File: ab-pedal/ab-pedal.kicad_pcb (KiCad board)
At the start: 2 copper layers, 52 x 70 mm, 24 parts, among them J2 IN, J3 OUT_A, J4 OUT_B, J5 IN_A, J6 IN_B, J7 OUT, J8 Jack-DC, SW1 TRUE_BYPASS, SW2 INVERT, SW3 ON, U1 TL074, U2 MAX1044

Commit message: layout
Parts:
- removed J3: OUT_A, Connector_Audio:Jack_6.35mm_Neutrik_NMJ6HFD2_Horizontal
- removed J5: IN_A, Connector_Audio:Jack_6.35mm_Neutrik_NMJ6HFD2_Horizontal
- added J1: PEDAL, Connector_Audio:Jack_6.35mm_Neutrik_NMJ6HFD2_Horizontal, B.Cu at (125.2, 123.7)
- C2, C4, C5: footprint Capacitor_THT:CP_Radial_D10.0mm_P5.00mm -> Capacitor_THT:CP_Radial_D4.0mm_P2.00mm
- J2, J7: moved to B.Cu
- J4: value OUT_B -> SEND; moved to B.Cu
- J6: value IN_B -> RECV; moved to B.Cu
- R1, R2, R3, R4, R5: footprint Resistor_THT:R_Axial_DIN0207_L6.3mm_D2.5mm_P10.16mm_Horizontal -> Resistor_THT:R_Axial_DIN0207_L6.3mm_D2.5mm_P5.08mm_Vertical
- SW3: footprint Connector_PinHeader_2.54mm:PinHeader_2x03_P2.54mm_Vertical -> _project:PinHeader_2x03_P2.54mm_Vertical
- moved SW3 187.5 mm to (55.9, 117.9), turned to 0 degrees
- moved D1 185.8 mm to (57.1, 106.4), turned to -90 degrees
- moved R5 179.4 mm to (61.8, 101.9), turned to 180 degrees
- moved J8 179.3 mm to (118.1, 119.9)
- moved R4 179.3 mm to (88.2, 104.1)
- moved C2 173.3 mm to (114.5, 121.2), turned to 180 degrees
- moved R3 171.0 mm to (97.1, 104.1)
- moved C5 161.8 mm to (108.7, 121.2)
- moved SW2 153.5 mm to (112.7, 87.1), turned to -90 degrees
- moved U1 148.1 mm to (98.3, 108.4), turned to -90 degrees
- moved C1 147.0 mm to (102.4, 109.8), turned to -90 degrees
- moved SW1 147.0 mm to (87.9, 87.3), turned to -90 degrees
- moved C3 144.2 mm to (118.1, 114.7), turned to 90 degrees
- moved R1 142.6 mm to (88.6, 120.3)
- moved R2 142.2 mm to (98.0, 120.3), turned to 0 degrees
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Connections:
- net IN_B renamed RETURN
- J2 pad R: (no net) -> GND
- J2 pad RN: (no net) -> GND
- J4 pad R: (no net) -> GND
- J4 pad RN: (no net) -> GND
- J4 pad T: OUT_A -> BUFFERED
- J6 pad R: (no net) -> GND
- J6 pad RN: (no net) -> GND
- J7 pad R: (no net) -> GND
- J7 pad RN: (no net) -> GND
- J7 pad TN: GND -> unconnected-(J7-PadTN)
- R1 pad 1: Net-(SW2B-A) -> Net-(SW2B-C)
- R1 pad 2: Net-(U1B--) -> Net-(U1D--)
- R2 pad 1: Net-(U1B--) -> Net-(U1D--)
- R2 pad 2: Net-(SW2A-A) -> Net-(SW2A-C)
- R3 pad 1: Net-(R3-Pad1) -> Net-(J1-PadR)
- R3 pad 2: Net-(U1C--) -> Net-(U1B--)
- R4 pad 1: Net-(U1C--) -> Net-(U1B--)
- RV1 pad 1: IN_A -> Net-(J1-PadSN)
- RV1 pad 2: Net-(R3-Pad1) -> Net-(J1-PadRN)
- RV1 pad 3: IN_B~ -> Net-(J1-PadTN)
- SW1 pad 1: IN_A -> Net-(SW1A-A)
- SW1 pad 2: Net-(SW1A-B) -> OUT
- SW1 pad 3: IN -> Net-(SW1A-C)
- SW1 pad 4: Net-(SW1B-A) -> BUFFERED
- SW1 pad 5: OUT -> Net-(SW1B-B)
- SW1 pad 6: Net-(SW1B-C) -> IN
- SW2 pad 2: IN_B~ -> RETURN~
- SW2 pad 4: Net-(SW2B-A) -> Net-(SW2A-A)
- SW2 pad 6: Net-(SW2A-C) -> Net-(SW2B-C)
- SW3 pad 1: BLEND -> Net-(D1-RK)
- SW3 pad 2: Net-(SW1B-C) -> GND
- SW3 pad 3: Net-(SW1A-B) -> Net-(D1-GK)
- SW3 pad 4: Net-(D1-RK) -> Net-(SW1B-B)
- SW3 pad 5: GND -> Net-(SW1A-C)
- SW3 pad 6: Net-(D1-GK) -> BLEND
- U1 pad 1: OUT_A -> Net-(SW1A-A)
- U1 pad 10: GND -> IN
- U1 pad 12: Net-(SW1B-C) -> GND
- U1 pad 13: Net-(SW1B-A) -> Net-(U1D--)
- U1 pad 14: Net-(SW1B-A) -> Net-(SW2A-C)
- U1 pad 2: OUT_A -> Net-(SW1A-A)
- U1 pad 3: IN -> Net-(SW1A-C)
- U1 pad 7: Net-(SW2A-A) -> BLEND
- U1 pad 8: BLEND -> BUFFERED
- U1 pad 9: Net-(U1C--) -> BUFFERED
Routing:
- net BUFFERED: track 0.00 -> 120.9 mm, vias 0 -> 1
- net +9V: track 0.00 -> 87.0 mm
- net IN: track 0.00 -> 84.9 mm
- net Net-(SW1A-C): track 0.00 -> 71.6 mm
- net BLEND: track 0.00 -> 53.3 mm
- net Net-(J1-PadR): track 0.00 -> 53.2 mm, vias 0 -> 1
- net Net-(SW1B-B): track 0.00 -> 49.2 mm
- net RETURN~: track 0.00 -> 46.0 mm
- net Net-(SW2B-C): track 0.00 -> 42.1 mm, vias 0 -> 1
- net Net-(SW2A-C): track 0.00 -> 39.4 mm, vias 0 -> 1
- net Net-(SW1A-A): track 0.00 -> 30.7 mm
- net Net-(J4-PadTN): track 0.00 -> 30.5 mm
- net Net-(J1-PadTN): track 0.00 -> 28.8 mm
- net Net-(J1-PadRN): track 0.00 -> 27.2 mm
- net Net-(J1-PadSN): track 0.00 -> 25.6 mm
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- added copper zone on B.Cu, net GND
- added copper zone on F.Cu, net GND
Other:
- board size 52 x 70 mm -> 96 x 52 mm

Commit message: update for mechanicals
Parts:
- J1, J2, J4, J6, J7: footprint Connector_Audio:Jack_6.35mm_Neutrik_NMJ6HFD2_Horizontal -> _project:Jack_6.35mm_Neutrik_NMJ6HCD3_Horizontal
- R5: value 1k -> 10k
- moved D1 26.3 mm to (63.0, 80.8)
- moved SW3 26.1 mm to (65.3, 93.5), turned to -90 degrees
- moved R5 24.9 mm to (65.3, 77.2)
- moved J1 14.5 mm to (138.9, 118.9)
- moved C1 13.2 mm to (115.6, 109.6)
- moved C3 13.2 mm to (131.3, 114.5)
- moved C4 13.2 mm to (131.5, 104.1)
- moved C5 13.2 mm to (121.9, 120.9)
- moved J8 13.2 mm to (131.3, 119.6)
- moved U2 13.2 mm to (127.5, 108.5)
- moved R1 13.2 mm to (101.8, 120.1)
- moved R2 13.2 mm to (111.2, 120.1)
- moved R3 13.2 mm to (110.3, 103.8)
- moved R4 13.2 mm to (101.4, 103.8)
- moved U1 13.2 mm to (111.5, 108.2)
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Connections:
- D1 pad 1: Net-(D1-A) -> Net-(D1-BK)
- D1 pad 2: Net-(D1-RK) -> unconnected-(D1-GK-Pad2)
- D1 pad 3: Net-(D1-GK) -> Net-(D1-A)
- D1 pad 4: unconnected-(D1-BK-Pad4) -> Net-(D1-RK)
- SW3 pad 3: Net-(D1-GK) -> Net-(D1-BK)
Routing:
- net Net-(SW1A-C): track 71.6 -> 13.4 mm
- net BUFFERED: track 120.9 -> 62.8 mm, vias 1 -> 0
- net Net-(SW1B-B): track 49.2 -> 0.00 mm
- net RETURN~: track 46.0 -> 0.00 mm
- net BLEND: track 53.3 -> 7.28 mm
- net Net-(J4-PadTN): track 30.5 -> 0.00 mm
- net Net-(J1-PadR): track 53.2 -> 24.7 mm, vias 1 -> 0
- net Net-(J1-PadSN): track 25.6 -> 0.00 mm
- net OUT: track 24.2 -> 0.00 mm
- net +9V: track 87.0 -> 66.5 mm
- net RETURN: track 19.2 -> 0.00 mm
- net Net-(D1-GK): track 13.7 -> 0.00 mm
- net IN: track 84.9 -> 73.7 mm
- net Net-(D1-RK): track 10.8 -> 0.00 mm
- net Net-(J1-PadRN): track 27.2 -> 18.6 mm
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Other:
- board size 96 x 52 mm -> 102.2 x 52 mm

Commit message: update layout
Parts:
- moved SW3 38.5 mm to (94.2, 118.9), turned to 0 degrees
- moved R5 21.0 mm to (74.2, 96.3)
- moved D1 4.60 mm to (59.8, 84.1), turned to 0 degrees
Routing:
- net Net-(D1-BK): track 0.00 -> 67.3 mm
- net Net-(D1-RK): track 0.00 -> 56.9 mm
- net RETURN~: track 0.00 -> 53.3 mm
- net BUFFERED: track 62.8 -> 116.0 mm
- net Net-(SW1B-B): track 0.00 -> 44.1 mm
- net Net-(SW1A-C): track 13.4 -> 47.1 mm, vias 0 -> 1
- net Net-(J1-PadSN): track 0.00 -> 28.8 mm
- net +9V: track 66.5 -> 91.5 mm
- net Net-(J1-PadR): track 24.7 -> 47.0 mm, vias 0 -> 1
- net OUT: track 0.00 -> 21.6 mm
- net RETURN: track 0.00 -> 16.8 mm
- net BLEND: track 7.28 -> 23.1 mm
- net Net-(D1-A): track 0.00 -> 14.3 mm
- net Net-(SW1A-A): track 26.0 -> 39.7 mm
- net IN: track 73.7 -> 86.0 mm
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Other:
- outline, holes or cut-outs redrawn

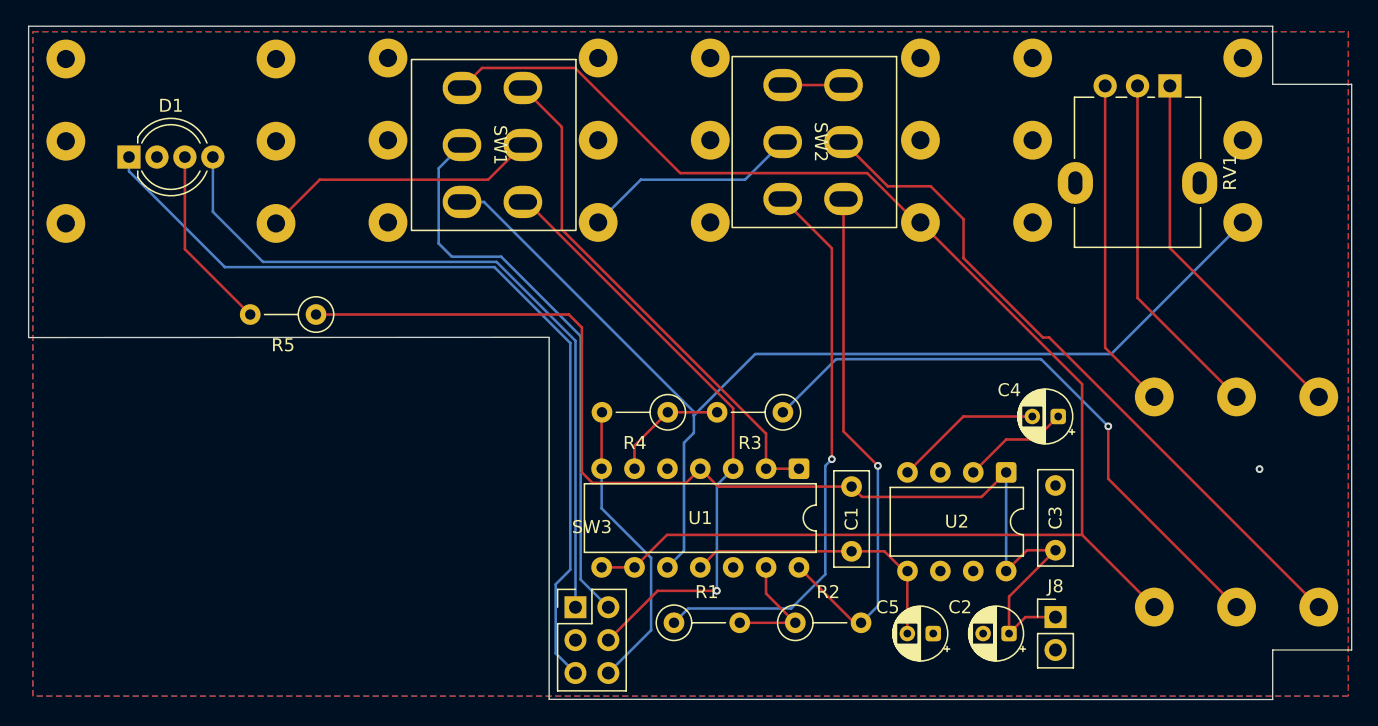
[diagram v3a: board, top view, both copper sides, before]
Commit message: add regulators
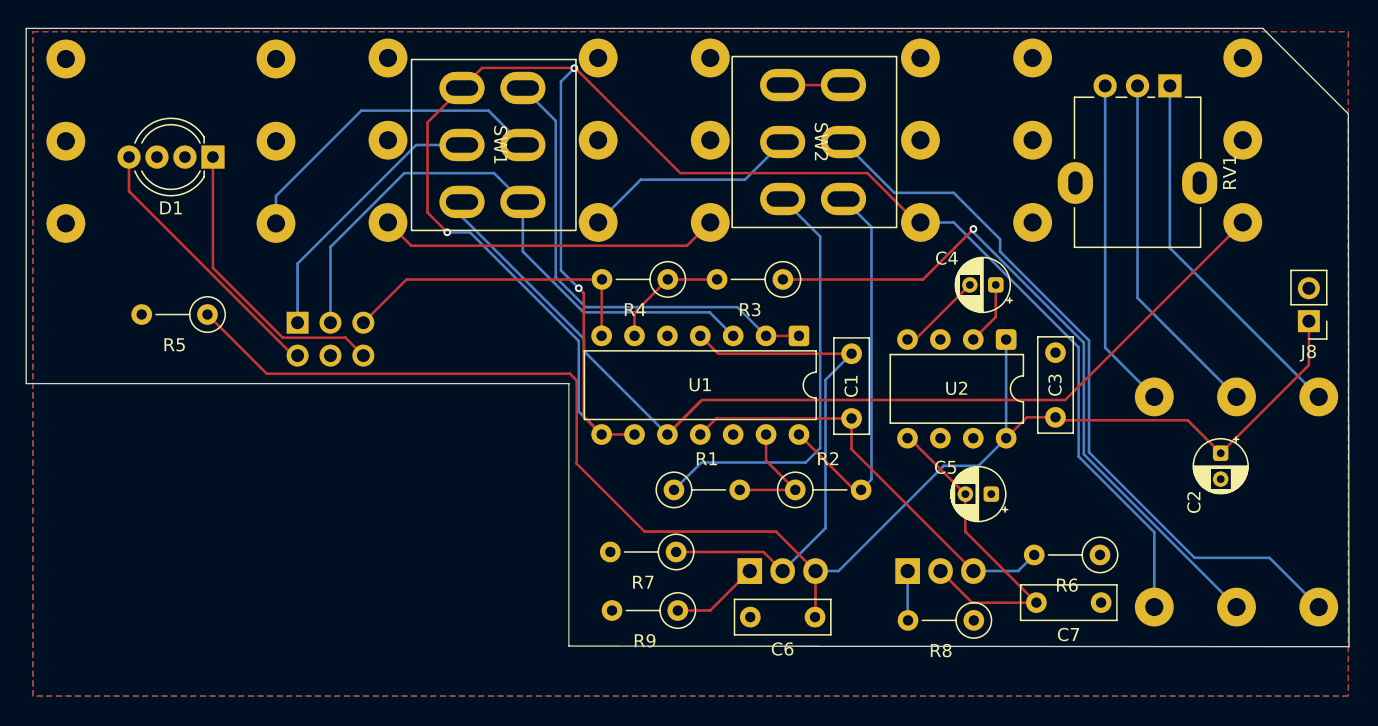
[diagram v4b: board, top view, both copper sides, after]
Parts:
- added C6: 100n, Capacitor_THT:C_Rect_L7.2mm_W2.5mm_P5.00mm_FKS2_FKP2_MKS2_MKP2, F.Cu at (112.7, 119.6)
- added C7: 100n, Capacitor_THT:C_Rect_L7.2mm_W2.5mm_P5.00mm_FKS2_FKP2_MKS2_MKP2, F.Cu at (134.8, 118.5)
- added R6: 220, Resistor_THT:R_Axial_DIN0207_L6.3mm_D2.5mm_P5.08mm_Vertical, F.Cu at (134.7, 114.8)
- added R7: 220, Resistor_THT:R_Axial_DIN0207_L6.3mm_D2.5mm_P5.08mm_Vertical, F.Cu at (102.0, 114.6)
- added R8: 1.2k, Resistor_THT:R_Axial_DIN0207_L6.3mm_D2.5mm_P5.08mm_Vertical, F.Cu at (125.0, 119.9)
- added R9: 1.2k, Resistor_THT:R_Axial_DIN0207_L6.3mm_D2.5mm_P5.08mm_Vertical, F.Cu at (102.1, 119.1)
- added U3: LM317_TO-220, Package_TO_SOT_THT:TO-220-3_Vertical, B.Cu at (107.7, 116.1)
- added U4: LM337_TO220, Package_TO_SOT_THT:TO-220-3_Vertical, B.Cu at (119.9, 116.1)
- SW3: moved to B.Cu
- moved SW3 30.7 mm to (72.8, 96.9), turned to -90 degrees
- moved J8 30.1 mm to (150.9, 96.8), turned to 180 degrees
- moved C2 21.5 mm to (144.1, 107.0), turned to -90 degrees
- moved C5 11.7 mm to (126.3, 110.1)
- moved C4 11.2 mm to (126.7, 94.0)
- moved C1 10.3 mm to (115.6, 99.3)
- moved R1 10.3 mm to (101.8, 109.8)
- moved R2 10.3 mm to (111.2, 109.8)
- moved R3 10.3 mm to (110.3, 93.6)
- moved R4 10.3 mm to (101.4, 93.6)
- moved U1 10.3 mm to (111.5, 97.9)
- moved U2 10.3 mm to (127.5, 98.2)
- moved C3 10.3 mm to (131.3, 104.2)
- moved R5 8.38 mm to (65.8, 96.3)
- moved D1 6.48 mm to (66.2, 84.1), turned to 180 degrees
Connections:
- C1 pad 1: +9V -> +7.5V
- C1 pad 2: -9V -> -7.5V
- SW3 pad 1: Net-(D1-RK) -> Net-(SW1B-B)
- SW3 pad 2: GND -> Net-(SW1A-C)
- SW3 pad 3: Net-(D1-BK) -> BLEND
- SW3 pad 4: Net-(SW1B-B) -> Net-(D1-RK)
- SW3 pad 5: Net-(SW1A-C) -> GND
- SW3 pad 6: BLEND -> Net-(D1-BK)
- U1 pad 11: -9V -> -7.5V
- U1 pad 4: +9V -> +7.5V
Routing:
- net Net-(D1-BK): track 67.3 -> 23.0 mm
- net +7.5V: track 0.00 -> 40.1 mm
- net Net-(D1-RK): track 56.9 -> 20.6 mm
- net -7.5V: track 0.00 -> 33.1 mm
- net BUFFERED: track 116.0 -> 146.4 mm, vias 0 -> 3
- net +9V: track 91.5 -> 120.1 mm
- net Net-(J4-PadTN): track 0.00 -> 26.4 mm
- net Net-(SW1B-B): track 44.1 -> 21.1 mm
- net Net-(D1-A): track 14.3 -> 0.00 mm
- net Net-(SW2B-C): track 44.0 -> 33.1 mm, vias 1 -> 0
- net Net-(SW2A-C): track 40.4 -> 29.7 mm, vias 1 -> 0
- net Net-(J1-PadR): track 47.0 -> 53.9 mm
- net Net-(U3-ADJ): track 0.00 -> 6.82 mm
- net IN: track 86.0 -> 79.4 mm
- net Net-(U2-CAP-): track 11.4 -> 5.96 mm
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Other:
- board size 102.2 x 52 mm -> 102.2 x 47.8 mm

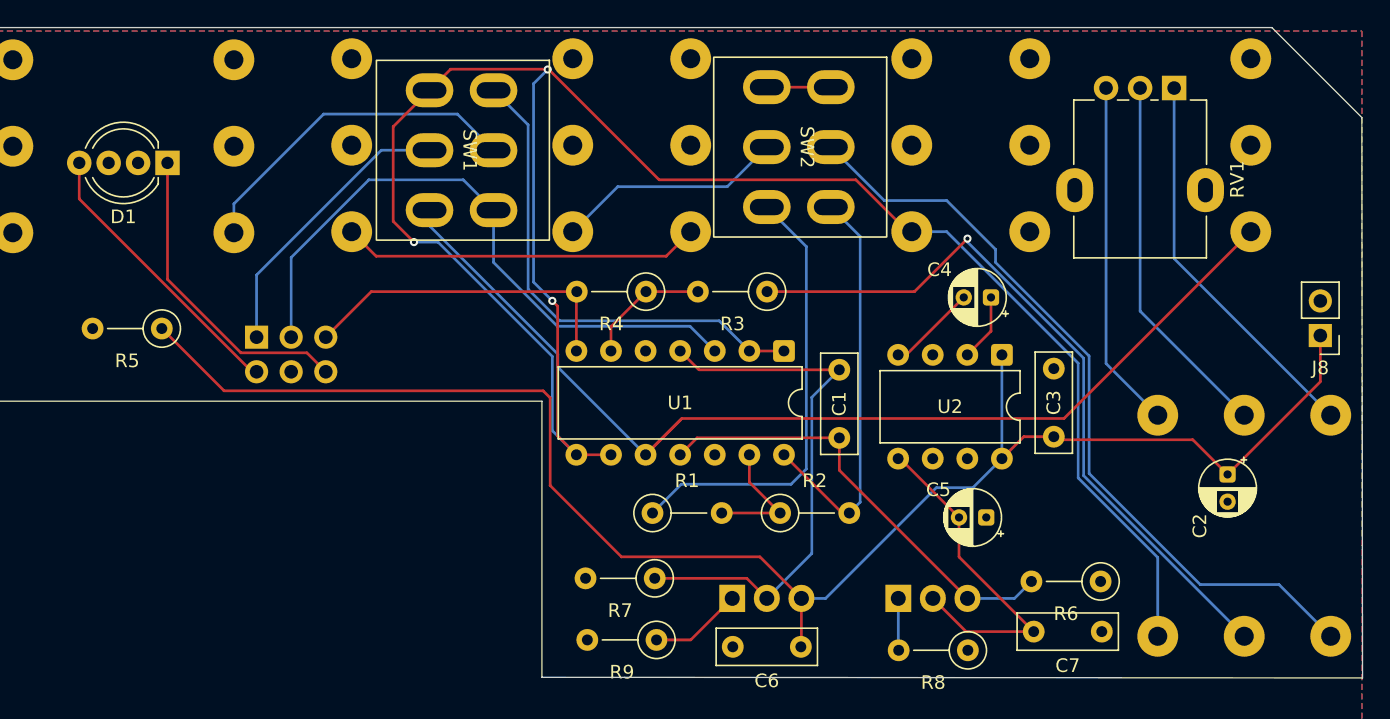
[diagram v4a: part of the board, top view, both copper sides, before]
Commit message: optimize nets
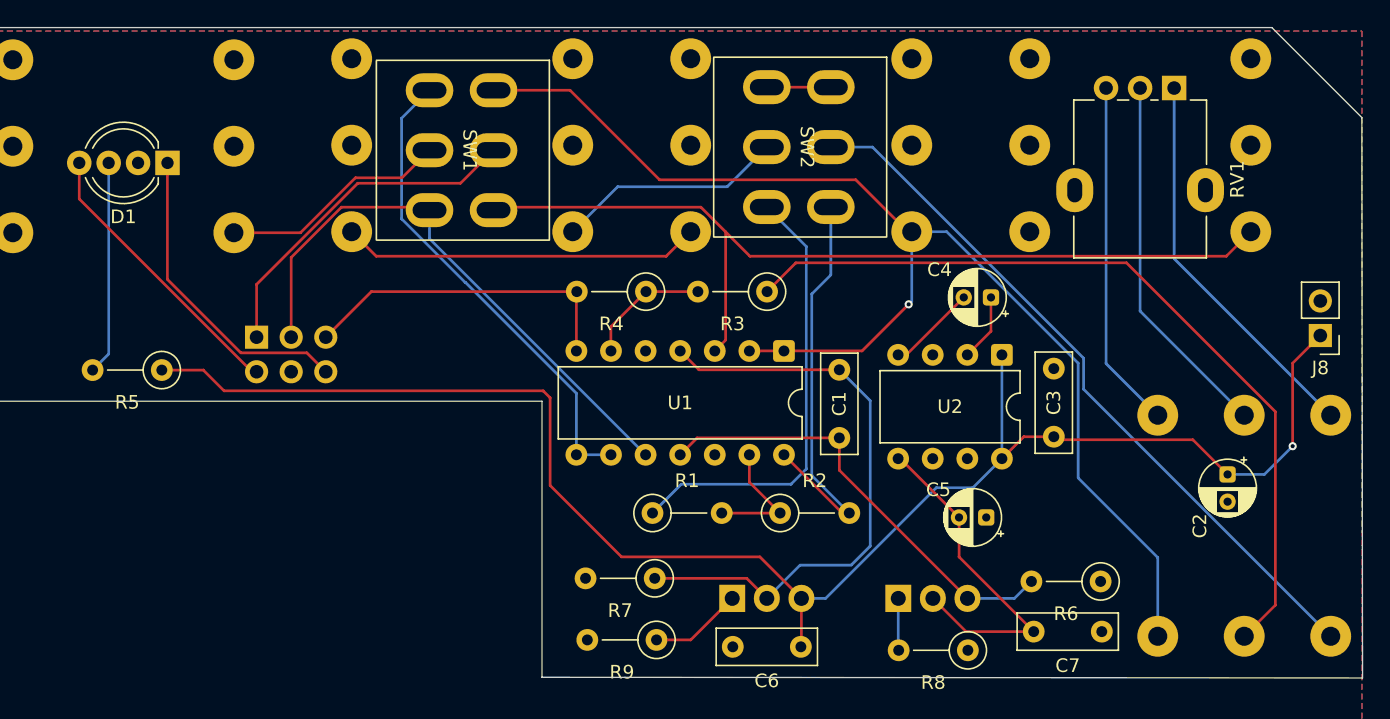
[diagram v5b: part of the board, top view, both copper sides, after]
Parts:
- moved R5 3.05 mm to (65.8, 99.3)
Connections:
- SW1 pad 1: Net-(SW1A-A) -> BUFFERED
- SW1 pad 2: OUT -> Net-(SW1A-B)
- SW1 pad 3: Net-(SW1A-C) -> IN
- SW1 pad 4: BUFFERED -> Net-(SW1B-A)
- SW1 pad 5: Net-(SW1B-B) -> OUT
- SW1 pad 6: IN -> Net-(SW1B-C)
- SW3 pad 1: Net-(SW1B-B) -> Net-(SW1A-B)
- SW3 pad 2: Net-(SW1A-C) -> Net-(SW1B-C)
- U1 pad 1: Net-(SW1A-A) -> BUFFERED
- U1 pad 10: IN -> Net-(SW1B-C)
- U1 pad 2: Net-(SW1A-A) -> BUFFERED
- U1 pad 3: Net-(SW1A-C) -> IN
- U1 pad 8: BUFFERED -> Net-(SW1B-A)
- U1 pad 9: BUFFERED -> Net-(SW1B-A)
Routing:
- net BUFFERED: track 146.4 -> 91.9 mm, vias 3 -> 1
- net Net-(SW1A-C): track 46.8 -> 0.00 mm
- net Net-(SW1B-C): track 0.00 -> 41.9 mm
- net Net-(SW1A-A): track 36.3 -> 0.00 mm
- net Net-(SW1B-A): track 0.00 -> 35.5 mm
- net Net-(SW1A-B): track 0.00 -> 25.4 mm
- net Net-(SW1B-B): track 21.1 -> 0.00 mm
- net Net-(D1-A): track 0.00 -> 15.7 mm
- net IN: track 79.4 -> 66.7 mm
- net OUT: track 25.0 -> 16.9 mm
- net Net-(J1-PadR): track 53.9 -> 60.2 mm, vias 1 -> 0
- net RETURN~: track 57.2 -> 52.9 mm
- net +7.5V: track 40.1 -> 44.2 mm
- net +9V: track 120.1 -> 120.4 mm, vias 0 -> 1
